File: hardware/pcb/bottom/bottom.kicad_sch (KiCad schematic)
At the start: 37 parts, among them J1 Conn_01x15_Socket

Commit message: migrate kicad projects from v8 to v9
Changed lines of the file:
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@@
 (kicad_sch
-	(version 20231120)
+	(version 20250114)
 	(generator "eeschema")
-	(generator_version "8.0")
+	(generator_version "9.0")
 	(paper "A4")
+	(rectangle
+		(start 68.58 25.4)
+		(end 124.46 85.09)
+		(stroke
+			(width 0)
+			(type default)
+		)
+		(fill
+			(type none)
+		)
+	)
+	(text "Bottom Board"
+		(exclude_from_sim no)
+		(at 227.33 174.498 0)
+		(effects
+			(font
+				(size 5.08 5.08)
+				(thickness 1.016)
+				(bold yes)
+			)
+		)
+	)
+	(text "Main Board"
+		(exclude_from_sim no)
+		(at 97.79 29.21 0)
+		(effects
+			(font
+				(size 2.54 2.54)
+				(thickness 0.508)
+				(bold yes)
+			)
+		)
+	)
+	(text "Adressable RGB LEDs"
+		(exclude_from_sim no)
+		(at 121.92 93.98 0)
+		(effects
+			(font
+				(size 2.54 2.54)
+				(thickness 0.508)
+				(bold yes)
+			)
+		)
+	)
+	(text "Decoupling Capacitor"
+		(exclude_from_sim no)
+		(at 187.706 68.326 0)
+		(effects
+			(font
+				(size 1.27 1.27)
+				(bold yes)
+			)
+		)
+	)
+	(text "Layout"
+		(exclude_from_sim no)
+		(at 187.96 91.694 0)
+		(effects
+			(font
+				(size 2.54 2.54)
+				(thickness 0.508)
+				(bold yes)
+			)
+		)
+	)
+	(text "Passives"
+		(exclude_from_sim no)
+		(at 189.484 28.956 0)
+		(effects
+			(font
+				(size 2.54 2.54)
+				(thickness 0.508)
+				(bold yes)
+			)
+		)
+	)
+	(text "Pull-up Resistors"
+		(exclude_from_sim no)
+		(at 187.96 34.036 0)
+		(effects
+			(font
+				(size 1.27 1.27)
+				(bold yes)
+			)
+		)
+	)
+	(text "Connection to \nTop Board"
+		(exclude_from_sim no)
+		(at 142.24 31.75 0)
+		(effects
+			(font
+				(size 2.54 2.54)
+				(thickness 0.508)
+				(bold yes)
+			)
+		)
+	)
 	(no_connect
 		(at 86.36 64.77)
@@
 		)
 	)
-	(rectangle
-		(start 68.58 25.4)
-		(end 124.46 85.09)
-		(stroke
-			(width 0)
-			(type default)
-		)
-		(fill
-			(type none)
-		)
-	)
-	(text "Bottom Board"
-		(exclude_from_sim no)
-		(at 227.33 174.498 0)
-		(effects
-			(font
-				(size 5.08 5.08)
-				(thickness 1.016)
-				(bold yes)
-			)
-		)
-	)
-	(text "Main Board"
-		(exclude_from_sim no)
-		(at 97.79 29.21 0)
-		(effects
-			(font
-				(size 2.54 2.54)
-				(thickness 0.508)
-				(bold yes)
-			)
-		)
-	)
-	(text "Adressable RGB LEDs"
-		(exclude_from_sim no)
-		(at 121.92 93.98 0)
-		(effects
-			(font
-				(size 2.54 2.54)
-				(thickness 0.508)
-				(bold yes)
-			)
-		)
-	)
-	(text "Decoupling Capacitor"
-		(exclude_from_sim no)
-		(at 187.706 68.326 0)
-		(effects
-			(font
-				(size 1.27 1.27)
-				(bold yes)
-			)
-		)
-	)
-	(text "Layout"
-		(exclude_from_sim no)
-		(at 187.96 91.694 0)
-		(effects
-			(font
-				(size 2.54 2.54)
-				(thickness 0.508)
-				(bold yes)
-			)
-		)
-	)
-	(text "Passives"
-		(exclude_from_sim no)
-		(at 189.484 28.956 0)
-		(effects
-			(font
-				(size 2.54 2.54)
-				(thickness 0.508)
-				(bold yes)
-			)
-		)
-	)
-	(text "Pull-up Resistors"
-		(exclude_from_sim no)
-		(at 187.96 34.036 0)
-		(effects
-			(font
-				(size 1.27 1.27)
-				(bold yes)
-			)
-		)
-	)
-	(text "Connection to \nTop Board"
-		(exclude_from_sim no)
-		(at 142.24 31.75 0)
-		(effects
-			(font
-				(size 2.54 2.54)
-				(thickness 0.508)
-				(bold yes)
-			)
-		)
-	)
 	(global_label "ROW2"
 		(shape input)
@@
 		(at 182.88 101.6 0)
 		(unit 1)
-		(exclude_from_sim yes)
+		(exclude_from_sim no)
 		(in_bom no)
 		(on_board yes)
@@
 		(at 191.77 101.6 0)
 		(unit 1)
-		(exclude_from_sim yes)
+		(exclude_from_sim no)
 		(in_bom no)
 		(on_board yes)
@@
 		(at 191.77 114.3 0)
 		(unit 1)
-		(exclude_from_sim yes)
+		(exclude_from_sim no)
 		(in_bom no)
 		(on_board yes)
@@
 		(at 182.88 114.3 0)
 		(unit 1)
-		(exclude_from_sim yes)
+		(exclude_from_sim no)
 		(in_bom no)
 		(on_board yes)
@@
 		)
 	)
+	(embedded_fonts no)
 )

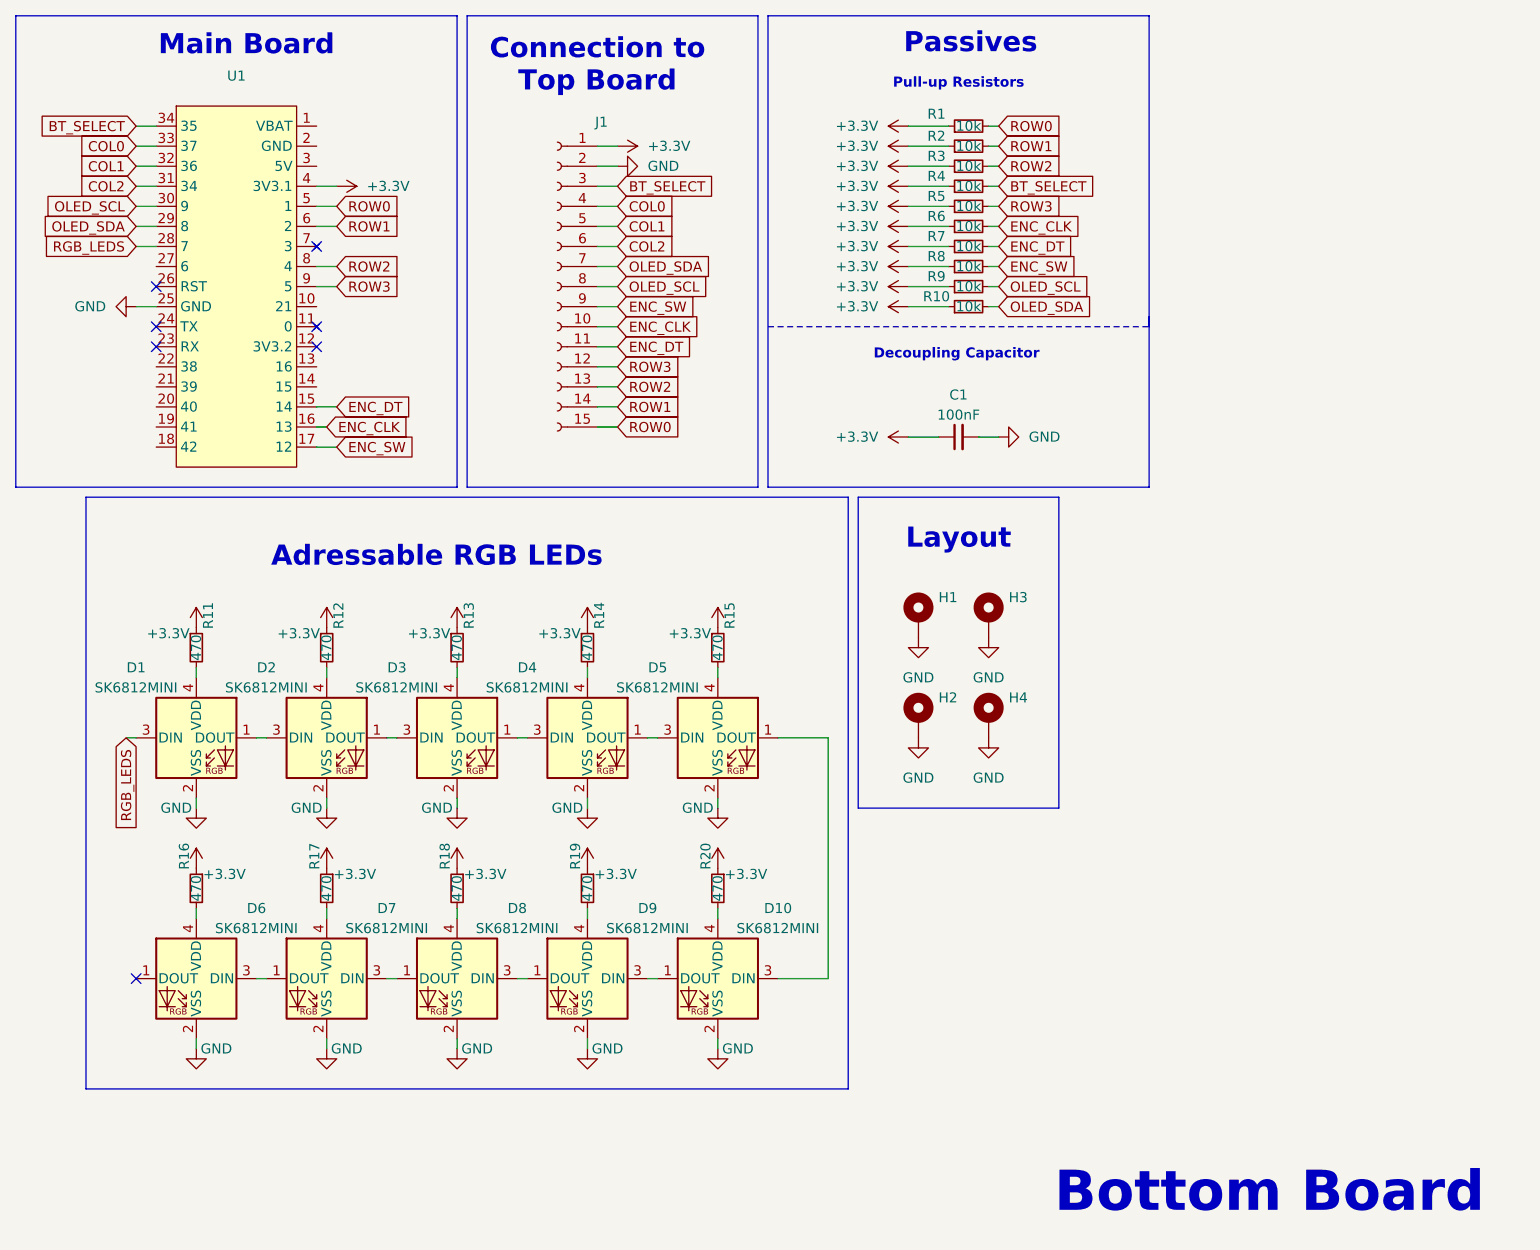
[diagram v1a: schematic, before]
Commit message: Optimize routing and improve grounding
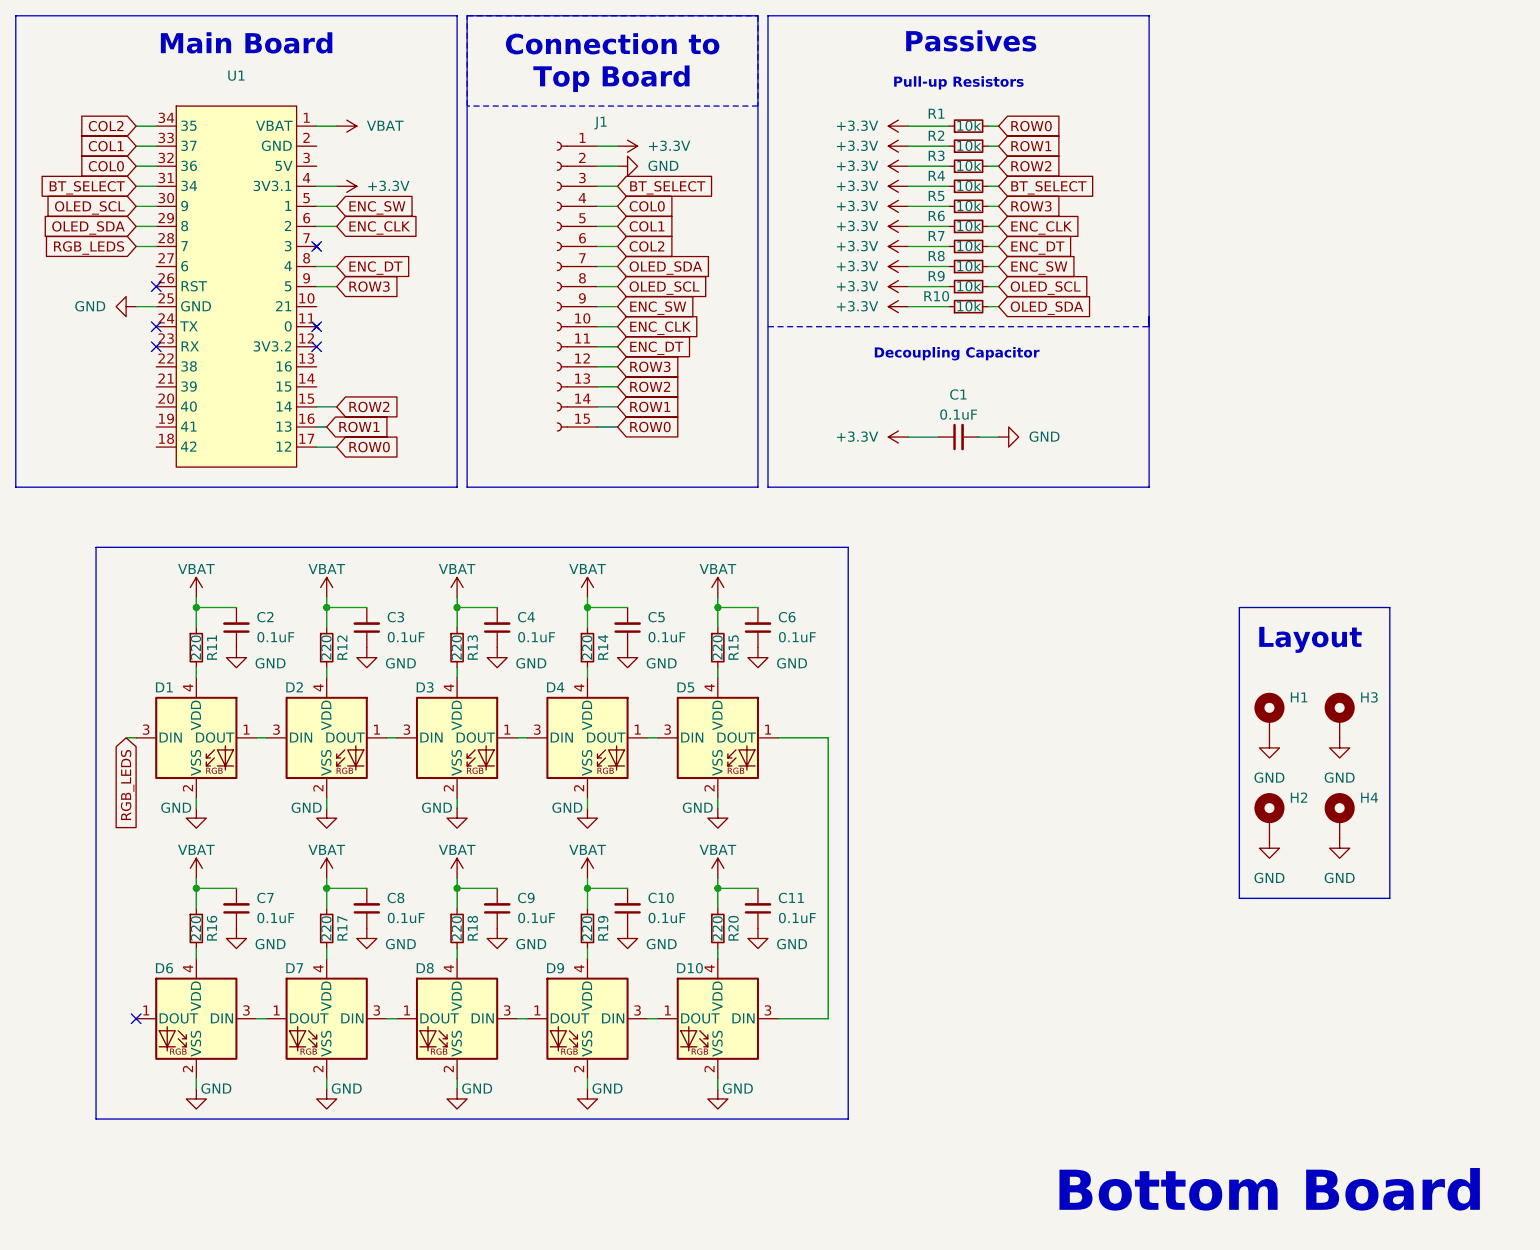
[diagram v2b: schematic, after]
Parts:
- added C10, C11, C2, C3, C4, C5, C6, C7, C8, C9: 0.1uF, Bottom-Footprints:C_0805_2012Metric_Pad1.18x1.45mm_HandSolder, symbol Bottom-Symbols:C_Small
- C1: value 100nF -> 0.1uF
- R11, R12, R13, R14, R15, R16, R17, R18, R19, R20: value 470 -> 220
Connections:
- net +3.3V: no longer R11.1, R12.1, R13.1, R14.1, R15.1, R16.1, R17.1, R18.1, R19.1, R20.1
- net BT_SELECT: now also U1.31 (34); no longer U1.34 (35)
- net COL0: now also U1.32 (36); no longer U1.33 (37)
- net COL1: now also U1.33 (37); no longer U1.32 (36)
- net COL2: now also U1.34 (35); no longer U1.31 (34)
- net ENC_CLK: now also U1.6 (2); no longer U1.16 (13)
- net ENC_DT: now also U1.8 (4); no longer U1.15 (14)
- net ENC_SW: now also U1.5 (1); no longer U1.17 (12)
- net GND: now also C10.1, C11.1, C2.1, C3.1, C4.1, C5.1, C6.1, C7.1, C8.1, C9.1
- net ROW0: now also U1.17 (12); no longer U1.5 (1)
- net ROW1: now also U1.16 (13); no longer U1.6 (2)
- net ROW2: now also U1.15 (14); no longer U1.8 (4)
- net VBAT: now reaches U1.1 (VBAT)
- net VBAT: now also R11.1, R12.1, R13.1, R14.1, R15.1, R16.1, R17.1, R18.1, R19.1, R20.1, C10.2, C11.2, C2.2, C3.2, C4.2, C5.2, C6.2, C7.2, C8.2, C9.2
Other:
- note removed: "Adressable RGB LEDs"
- note removed: "Connection to Top Board"
- moved on the sheet: D10, D6, D7, D8, D9, H1, H2, H3, H4

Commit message: wip
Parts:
- D1, D10, D2, D3, D4, D5, D6, D7, D8, D9: footprint Bottom-Footprints:LED_SK6812MINI_PLCC4_3.5x3.5mm_P1.75mm -> Bottom-Footprints:SK6812-MINI-E
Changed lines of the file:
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@@
 			)
 		)
-		(property "Footprint" "Bottom-Footprints:LED_SK6812MINI_PLCC4_3.5x3.5mm_P1.75mm"
+		(property "Footprint" "Bottom-Footprints:SK6812-MINI-E"
 			(at 92.71 124.46 0)
 			(effects
@@
 			)
 		)
-		(property "Footprint" "Bottom-Footprints:LED_SK6812MINI_PLCC4_3.5x3.5mm_P1.75mm"
+		(property "Footprint" "Bottom-Footprints:SK6812-MINI-E"
 			(at 123.19 160.02 0)
 			(effects
@@
 			)
 		)
-		(property "Footprint" "Bottom-Footprints:LED_SK6812MINI_PLCC4_3.5x3.5mm_P1.75mm"
+		(property "Footprint" "Bottom-Footprints:SK6812-MINI-E"
 			(at 106.68 160.02 0)
 			(effects
@@
 			)
 		)
-		(property "Footprint" "Bottom-Footprints:LED_SK6812MINI_PLCC4_3.5x3.5mm_P1.75mm"
+		(property "Footprint" "Bottom-Footprints:SK6812-MINI-E"
 			(at 142.24 124.46 0)
 			(effects
@@
 			)
 		)
-		(property "Footprint" "Bottom-Footprints:LED_SK6812MINI_PLCC4_3.5x3.5mm_P1.75mm"
+		(property "Footprint" "Bottom-Footprints:SK6812-MINI-E"
 			(at 156.21 160.02 0)
 			(effects
@@
 			)
 		)
-		(property "Footprint" "Bottom-Footprints:LED_SK6812MINI_PLCC4_3.5x3.5mm_P1.75mm"
+		(property "Footprint" "Bottom-Footprints:SK6812-MINI-E"
 			(at 109.22 124.46 0)
 			(effects
@@
 			)
 		)
-		(property "Footprint" "Bottom-Footprints:LED_SK6812MINI_PLCC4_3.5x3.5mm_P1.75mm"
+		(property "Footprint" "Bottom-Footprints:SK6812-MINI-E"
 			(at 158.75 124.46 0)
 			(effects
@@
 			)
 		)
-		(property "Footprint" "Bottom-Footprints:LED_SK6812MINI_PLCC4_3.5x3.5mm_P1.75mm"
+		(property "Footprint" "Bottom-Footprints:SK6812-MINI-E"
 			(at 125.73 124.46 0)
 			(effects
@@
 			)
 		)
-		(property "Footprint" "Bottom-Footprints:LED_SK6812MINI_PLCC4_3.5x3.5mm_P1.75mm"
+		(property "Footprint" "Bottom-Footprints:SK6812-MINI-E"
 			(at 139.7 160.02 0)
 			(effects
@@
 			)
 		)
-		(property "Footprint" "Bottom-Footprints:LED_SK6812MINI_PLCC4_3.5x3.5mm_P1.75mm"
+		(property "Footprint" "Bottom-Footprints:SK6812-MINI-E"
 			(at 90.17 160.02 0)
 			(effects
